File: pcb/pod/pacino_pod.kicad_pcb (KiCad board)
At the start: 2 copper layers, 139.1 x 114.2 mm, 47 parts, among them SW1 MX_Hotswap_Rev, SW10 MX_Hotswap_Rev, SW11 MX_Hotswap_Rev, SW12 MX_Hotswap_Rev, SW13 MX_Hotswap_Rev, SW14 MX_Hotswap_Rev, SW15 MX_Hotswap_Rev, SW16 MX_Hotswap_Rev, SW17 MX_Hotswap_Rev, SW18 MX_Hotswap_Rev, SW19 MX_Hotswap_Rev, SW2 MX_Hotswap_Rev, SW20 MX_Hotswap_Rev, SW3 MX_Hotswap_Rev, SW4 MX_Hotswap_Rev, SW5 MX_Hotswap_Rev, SW6 MX_Hotswap_Rev, SW7 MX_Hotswap_Rev, SW8 MX_Hotswap_Rev, SW9 MX_Hotswap_Rev, U1 nice!nano

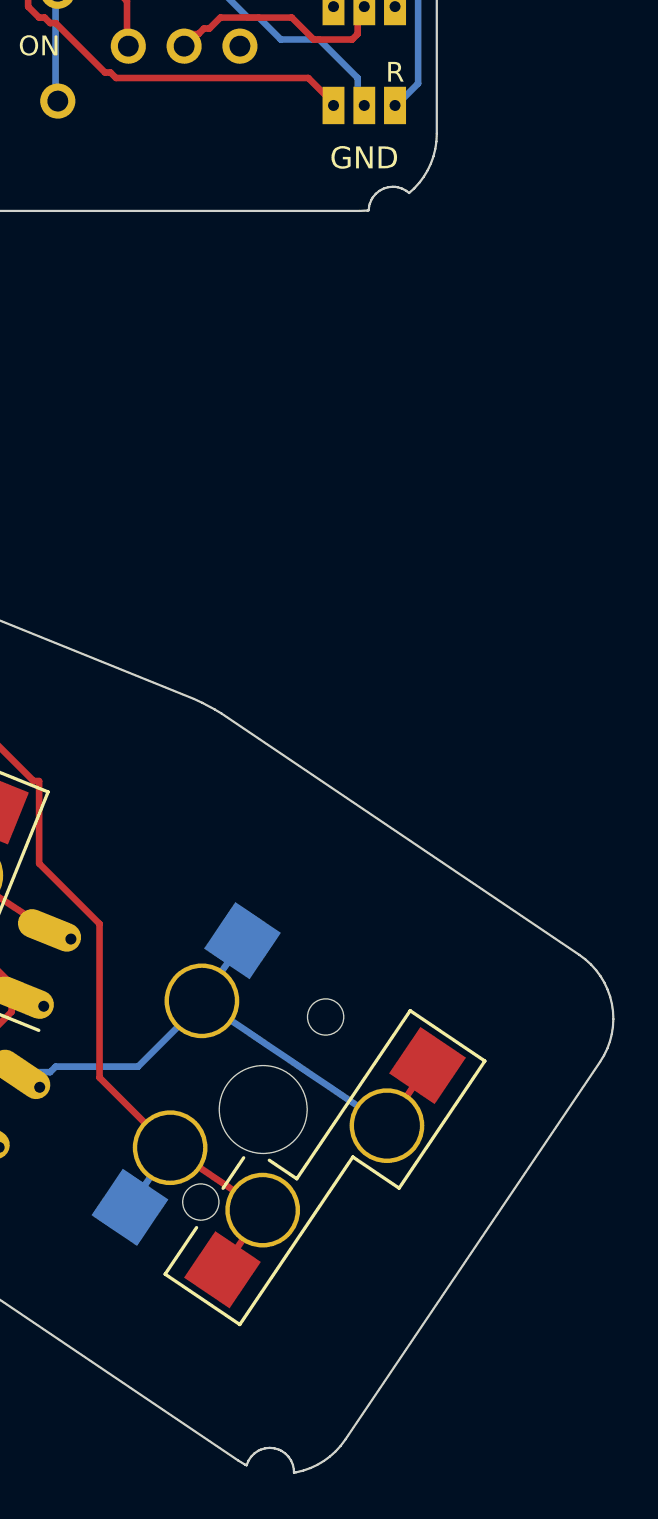
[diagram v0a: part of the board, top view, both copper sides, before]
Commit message: Slim build: screw channels up the wall over the insert holes, 3 mm wall, three pillars pulled in
The pillars stop at the board while the wall keeps rising 5 mm past them, so the seven insert
holes on the wall line were tucked 1.2 mm under it: a half-moon from above, no way in for an
insert, and the screws would have sat 0.5 mm into the wall. Now a 4 mm channel (pcb_screw_channel)
runs up the inside of the wall over each hole, the slim case's wall is 3 mm (pcb_wall) so 1.5 mm
is left behind it, and the three pillars with room (thumb end, the bay's bottom corner, the one by
the thumb keys already was) stand 2.5-3 mm clear of the wall as full round bosses. Both boards
regenerated (five edge notches, three real holes); hand-wired builds unchanged.

Co-Authored-By: Claude Fable 5 <noreply@anthropic.com>
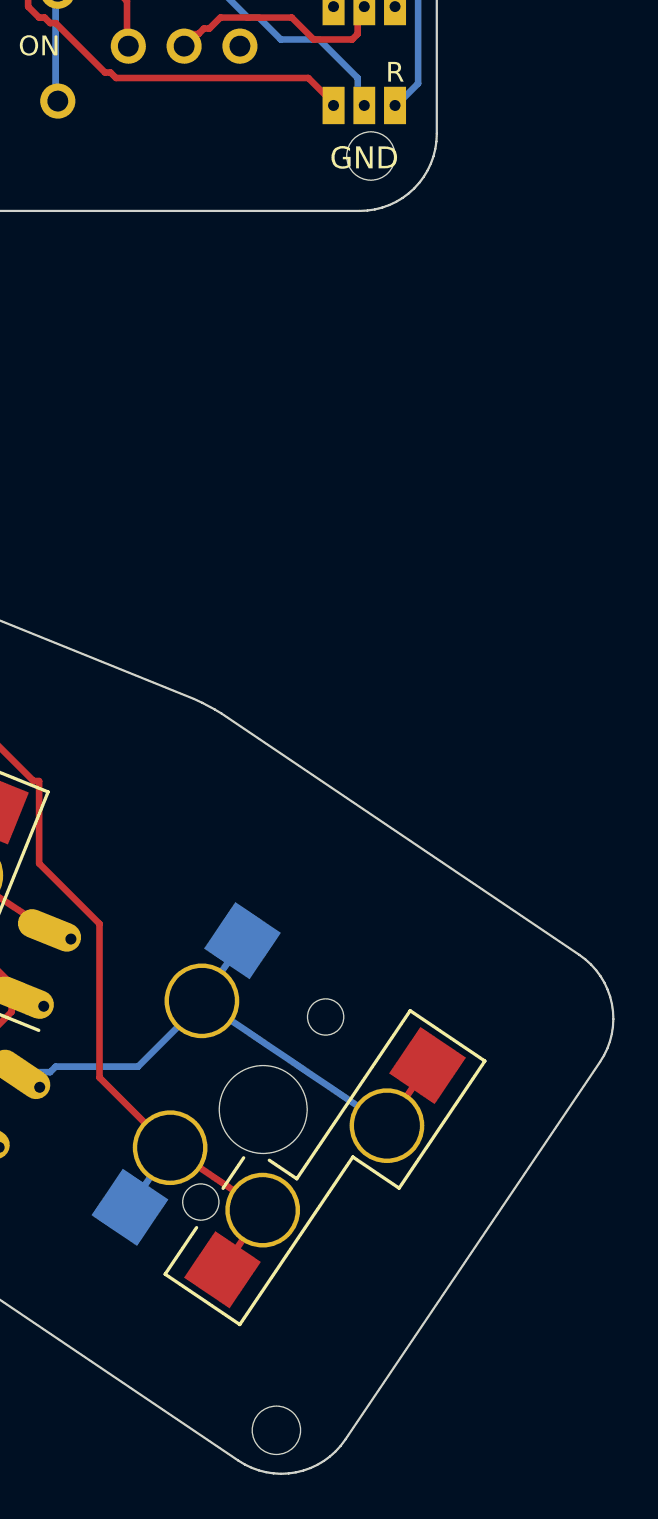
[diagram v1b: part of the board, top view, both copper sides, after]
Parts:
- added H2: MountingHole, pacino_pod:MountingHole, F.Cu at (176.6, 108.3)
- added H3: MountingHole, pacino_pod:MountingHole, F.Cu at (118.5, 124.4)
- moved H1 68.2 mm to (172.3, 166.3)
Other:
- board size 139.1 x 114.2 mm -> 139.1 x 114.3 mm

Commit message: PCB: controller on top of the board, reset legs paired the right way, jumpers clear of the boss
Three things the first batch of boards taught us:

- The nano sits on the face opposite the sockets (on top, flush in the plate window --
  what the case is built around), which swaps its pin rows relative to what the generator
  assumed. Per-half pin tables, the printed ZMK lists (right half columns inner-first) and
  the L/R silkscreen faces are now computed for that; MCU power nets renamed so the L pads
  serve the left half.
- A 12 mm tactile links its two legs 12.5 mm apart internally; the footprint had the 5 mm
  pairs on one net, so a normally fitted switch held RST at GND and the nano never booted.
- JP1/JP2 sat 2.3 mm from the bay's corner mounting hole, under its boss: a bridge there
  keeps the case from closing. Moved 4.5 mm up the strip, with a clearance guard.

Also: the nice!view goes on pro_micro 1/2/3 (ZMK's adapter), not 14/15/16 -- the hand-wired
build needs no rewiring; on the PCB a display needs its own SPI pins. Boards, gerbers,
renders and READMEs regenerated; overlays match the zmk-config copies.

Co-Authored-By: Claude Fable 5.1 <noreply@anthropic.com>
Claude-Session: https://claude.ai/code/session_01BAXTGjnxuhw6nNKSjTcvZb
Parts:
- moved JP1 4.50 mm to (176.3, 97.0)
- moved JP2 4.50 mm to (176.3, 101.5)
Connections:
- U1 pad 1: BAT_R -> BAT_L
- U1 pad 21: GND_R -> GND_L
- U1 pad 24: BAT_L -> BAT_R
- U1 pad 4: GND_L -> GND_R
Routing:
- net RST_B: track 41.5 -> 54.0 mm, vias 1 -> 2
- net GND_L: track 49.7 -> 37.3 mm, vias 0 -> 1
- net BAT_R: track 48.5 -> 37.7 mm
- net GND_R: track 39.8 -> 48.2 mm
- net COL3: track 169.4 -> 177.4 mm
- net RST_A: track 40.3 -> 47.8 mm
- net COL2: track 205.4 -> 210.6 mm
- net COL4: track 156.2 -> 159.9 mm, vias 1 -> 3
- net ROW4: track 96.7 -> 93.8 mm, vias 1 -> 2
- net BAT_L: track 41.1 -> 43.3 mm
- net COL0: track 174.0 -> 176.0 mm, vias 1 -> 0
- net COL1: track 172.8 -> 174.9 mm, vias 3 -> 1
- net GND: track 17.4 -> 15.5 mm
- net ROW0: track 141.0 -> 139.6 mm
- net BAT_SW: track 10.4 -> 11.4 mm
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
